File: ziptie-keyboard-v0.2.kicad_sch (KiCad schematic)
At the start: 147 parts, among them SW1 RotaryEncoder, U1 nice_nano

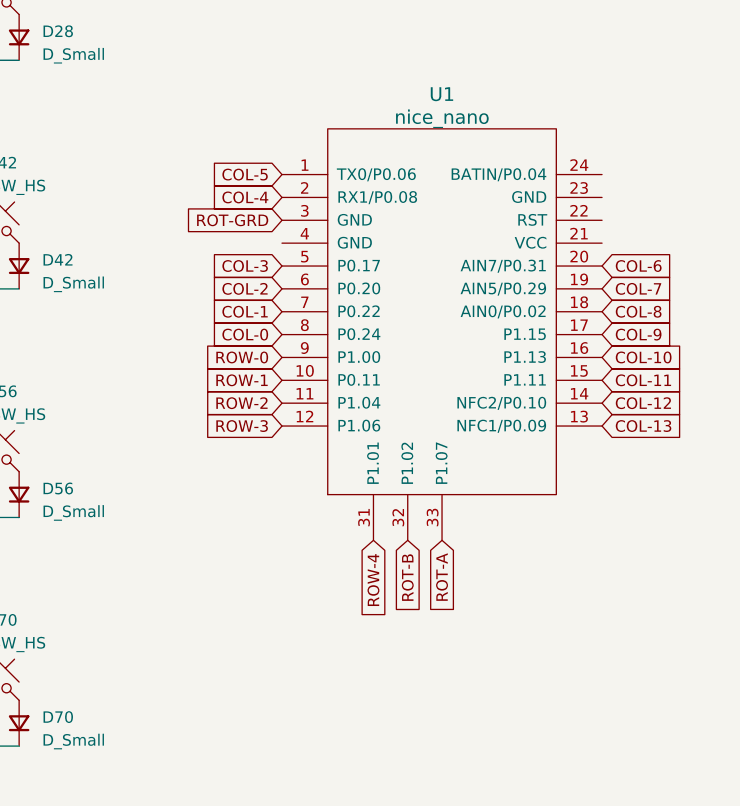
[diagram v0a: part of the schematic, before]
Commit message: Updated traces to 1mm and traced matrix
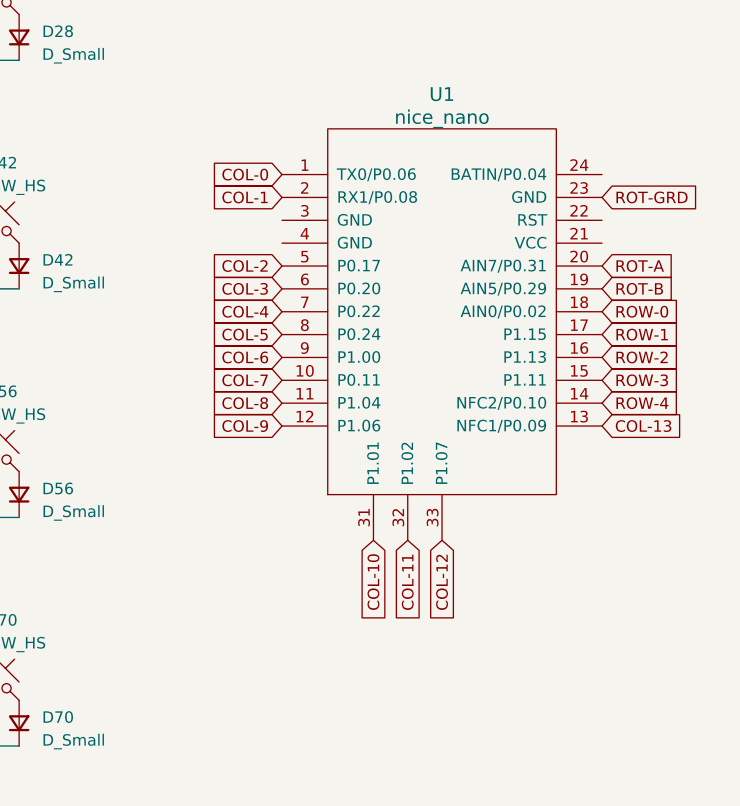
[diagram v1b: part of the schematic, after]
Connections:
- net COL-0: now also U1.1 (TX0/P0.06); no longer U1.8 (P0.24)
- net COL-1: now also U1.2 (RX1/P0.08); no longer U1.7 (P0.22)
- net COL-10: now also U1.31 (P1.01); no longer U1.16 (P1.13)
- net COL-11: now also U1.32 (P1.02); no longer U1.15 (P1.11)
- net COL-12: now also U1.33 (P1.07); no longer U1.14 (NFC2/P0.10)
- net COL-2: now also U1.5 (P0.17); no longer U1.6 (P0.20)
- net COL-3: now also U1.6 (P0.20); no longer U1.5 (P0.17)
- net COL-4: now also U1.7 (P0.22); no longer U1.2 (RX1/P0.08)
- net COL-5: now also U1.8 (P0.24); no longer U1.1 (TX0/P0.06)
- net COL-6: now also U1.9 (P1.00); no longer U1.20 (AIN7/P0.31)
- net COL-7: now also U1.10 (P0.11); no longer U1.19 (AIN5/P0.29)
- net COL-8: now also U1.11 (P1.04); no longer U1.18 (AIN0/P0.02)
- net COL-9: now also U1.12 (P1.06); no longer U1.17 (P1.15)
- net ROT-A: now also U1.20 (AIN7/P0.31); no longer U1.33 (P1.07)
- net ROT-B: now also U1.19 (AIN5/P0.29); no longer U1.32 (P1.02)
- net ROT-GRD: now also U1.23 (GND); no longer U1.3 (GND)
- net ROW-0: now also U1.18 (AIN0/P0.02); no longer U1.9 (P1.00)
- net ROW-1: now also U1.17 (P1.15); no longer U1.10 (P0.11)
- net ROW-2: now also U1.16 (P1.13); no longer U1.11 (P1.04)
- net ROW-3: now also U1.15 (P1.11); no longer U1.12 (P1.06)
- net ROW-4: now also U1.14 (NFC2/P0.10); no longer U1.31 (P1.01)

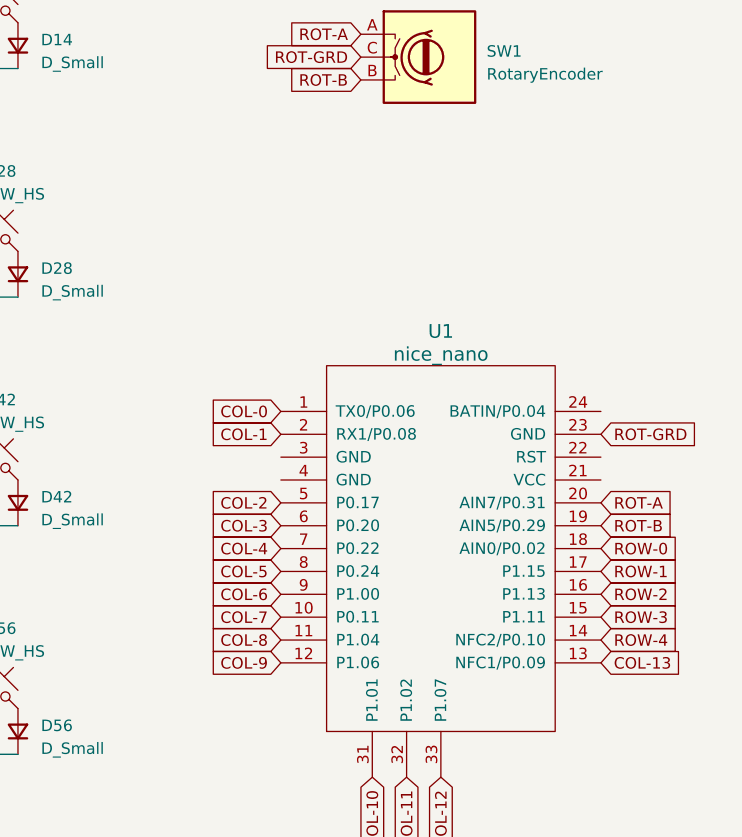
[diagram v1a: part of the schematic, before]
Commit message: Added traces and board cuts
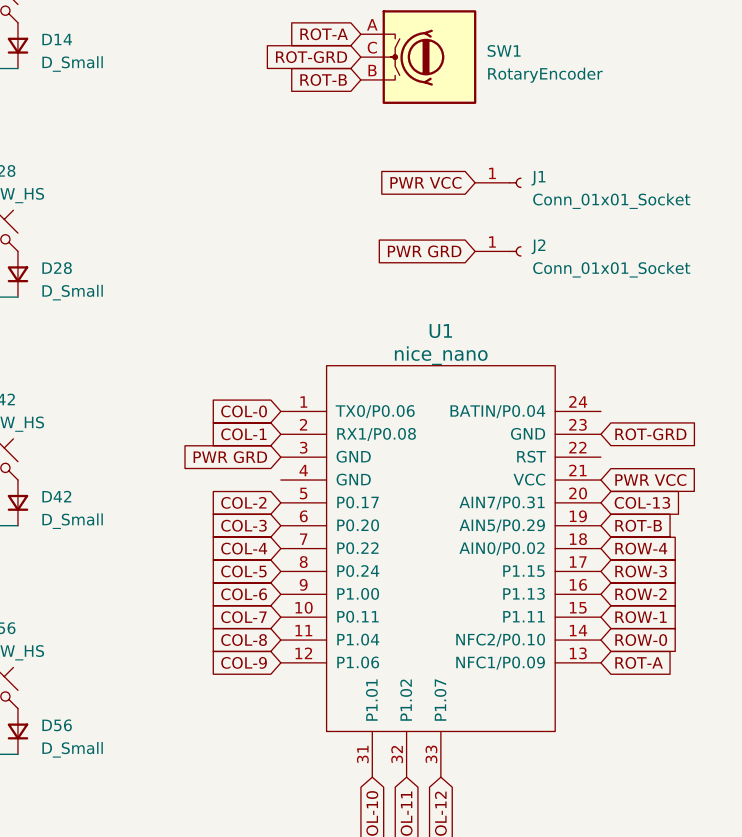
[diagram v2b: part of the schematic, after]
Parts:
- added J1, J2: Conn_01x01_Socket, Connector_Wire:SolderWire-0.1sqmm_1x01_D0.4mm_OD1mm, symbol Connector:Conn_01x01_Socket
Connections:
- net COL-13: now also U1.20 (AIN7/P0.31); no longer U1.13 (NFC1/P0.09)
- net ROT-A: now also U1.13 (NFC1/P0.09); no longer U1.20 (AIN7/P0.31)
- net ROW-0: now also U1.14 (NFC2/P0.10); no longer U1.18 (AIN0/P0.02)
- net ROW-1: now also U1.15 (P1.11); no longer U1.17 (P1.15)
- net ROW-3: now also U1.17 (P1.15); no longer U1.15 (P1.11)
- net ROW-4: now also U1.18 (AIN0/P0.02); no longer U1.14 (NFC2/P0.10)
- net PWR VCC: now reaches U1.21 (VCC)
- net PWR VCC: now also J1.1 (Pin_1)
- net PWR GRD: now reaches U1.3 (GND)
- net PWR GRD: now also J2.1 (Pin_1)
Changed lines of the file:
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@@
+    )
+  )
+  (global_label "PWR GRD" (shape input) (at 229.87 91.44 180) (fields_autoplaced)
+    (effects (font (size 1.27 1.27)) (justify right))
+    (property "Intersheetrefs" "${INTERSHEET_REFS}" (at 218.1952 91.44 0)
+      (effects (font (size 1.27 1.27)) (justify right) hide)
     )
   )
@@
     )
   )
-  (global_label "ROT-A" (shape input) (at 265.43 96.52 0) (fields_autoplaced)
+  (global_label "PWR VCC" (shape input) (at 265.43 93.98 0) (fields_autoplaced)
     (effects (font (size 1.27 1.27)) (justify left))
-    (property "Intersheetrefs" "${INTERSHEET_REFS}" (at 274.5649 96.52 0)
+    (property "Intersheetrefs" "${INTERSHEET_REFS}" (at 276.9234 93.98 0)
+      (effects (font (size 1.27 1.27)) (justify left) hide)
+    )
+  )
+  (global_label "ROT-A" (shape input) (at 265.43 114.3 0) (fields_autoplaced)
+    (effects (font (size 1.27 1.27)) (justify left))
+    (property "Intersheetrefs" "${INTERSHEET_REFS}" (at 274.5649 114.3 0)
       (effects (font (size 1.27 1.27)) (justify left) hide)
     )
@@
     )
   )
-  (global_label "ROW-3" (shape input) (at 265.43 109.22 0) (fields_autoplaced)
+  (global_label "ROW-3" (shape input) (at 265.43 104.14 0) (fields_autoplaced)
     (effects (font (size 1.27 1.27)) (justify left))
-    (property "Intersheetrefs" "${INTERSHEET_REFS}" (at 275.1696 109.22 0)
+    (property "Intersheetrefs" "${INTERSHEET_REFS}" (at 275.1696 104.14 0)
       (effects (font (size 1.27 1.27)) (justify left) hide)
     )
@@
     )
   )
-  (global_label "COL-13" (shape input) (at 265.43 114.3 0) (fields_autoplaced)
+  (global_label "PWR VCC" (shape input) (at 251.46 60.96 180) (fields_autoplaced)
+    (effects (font (size 1.27 1.27)) (justify right))
+    (property "Intersheetrefs" "${INTERSHEET_REFS}" (at 239.9666 60.96 0)
+      (effects (font (size 1.27 1.27)) (justify right) hide)
+    )
+  )
+  (global_label "COL-13" (shape input) (at 265.43 96.52 0) (fields_autoplaced)
     (effects (font (size 1.27 1.27)) (justify left))
-    (property "Intersheetrefs" "${INTERSHEET_REFS}" (at 275.9558 114.3 0)
+    (property "Intersheetrefs" "${INTERSHEET_REFS}" (at 275.9558 96.52 0)
       (effects (font (size 1.27 1.27)) (justify left) hide)
     )
   )
-  (global_label "ROW-1" (shape input) (at 265.43 104.14 0) (fields_autoplaced)
+  (global_label "ROW-1" (shape input) (at 265.43 109.22 0) (fields_autoplaced)
     (effects (font (size 1.27 1.27)) (justify left))
-    (property "Intersheetrefs" "${INTERSHEET_REFS}" (at 275.1696 104.14 0)
+    (property "Intersheetrefs" "${INTERSHEET_REFS}" (at 275.1696 109.22 0)
       (effects (font (size 1.27 1.27)) (justify left) hide)
     )
@@
     )
   )
-  (global_label "ROW-0" (shape input) (at 265.43 101.6 0) (fields_autoplaced)
+  (global_label "ROW-0" (shape input) (at 265.43 111.76 0) (fields_autoplaced)
     (effects (font (size 1.27 1.27)) (justify left))
-    (property "Intersheetrefs" "${INTERSHEET_REFS}" (at 275.1696 101.6 0)
+    (property "Intersheetrefs" "${INTERSHEET_REFS}" (at 275.1696 111.76 0)
       (effects (font (size 1.27 1.27)) (justify left) hide)
     )
@@
     )
   )
-  (global_label "ROW-4" (shape input) (at 265.43 111.76 0) (fields_autoplaced)
+  (global_label "ROW-4" (shape input) (at 265.43 101.6 0) (fields_autoplaced)
     (effects (font (size 1.27 1.27)) (justify left))
-    (property "Intersheetrefs" "${INTERSHEET_REFS}" (at 275.1696 111.76 0)
+    (property "Intersheetrefs" "${INTERSHEET_REFS}" (at 275.1696 101.6 0)
       (effects (font (size 1.27 1.27)) (justify left) hide)
     )
@@
     (property "Intersheetrefs" "${INTERSHEET_REFS}" (at 132.08 21.1637 90)
       (effects (font (size 1.27 1.27)) (justify left) hide)
+    )
+  )
+  (global_label "PWR GRD" (shape input) (at 251.46 68.58 180) (fields_autoplaced)
+    (effects (font (size 1.27 1.27)) (justify right))
+    (property "Intersheetrefs" "${INTERSHEET_REFS}" (at 239.7852 68.58 0)
+      (effects (font (size 1.27 1.27)) (justify right) hide)
     )
   )
@@
     )
   )
+  (symbol (lib_id "Connector:Conn_01x01_Socket") (at 256.54 60.96 0) (unit 1)
+    (in_bom yes) (on_board yes) (dnp no) (fields_autoplaced)
+    (property "Reference" "J1" (at 257.81 60.325 0)
+      (effects (font (size 1.27 1.27)) (justify left))
+    )
+    (property "Value" "Conn_01x01_Socket" (at 257.81 62.865 0)
+      (effects (font (size 1.27 1.27)) (justify left))
+    )
+    (property "Footprint" "Connector_Wire:SolderWire-0.1sqmm_1x01_D0.4mm_OD1mm" (at 256.54 60.96 0)
+      (effects (font (size 1.27 1.27)) hide)
+    )
+    (property "Datasheet" "~" (at 256.54 60.96 0)
+      (effects (font (size 1.27 1.27)) hide)
+    )
+    (pin "1")
+    (instances
+      (project "ziptie-keyboard-v0.2"
+        (path "/32677d6d-f5c2-46e9-b63f-fb92156b1d8b"
+          (reference "J1") (unit 1)
+        )
+      )
+    )
+  )
   (symbol (lib_id "marbastlib-choc:choc_SW_HS") (at 121.92 142.24 0) (unit 1)
     (in_bom yes) (on_board yes) (dnp no) (fields_autoplaced)
@@
         )
       )
+    )
+  )
+  (symbol (lib_id "Connector:Conn_01x01_Socket") (at 256.54 68.58 0) (unit 1)
+    (in_bom yes) (on_board yes) (dnp no) (fields_autoplaced)
+    (property "Reference" "J2" (at 257.81 67.945 0)
+      (effects (font (size 1.27 1.27)) (justify left))
+    )
+    (property "Value" "Conn_01x01_Socket" (at 257.81 70.485 0)
+      (effects (font (size 1.27 1.27)) (justify left))
+    )
+    (property "Footprint" "Connector_Wire:SolderWire-0.1sqmm_1x01_D0.4mm_OD1mm" (at 256.54 68.58 0)
+      (effects (font (size 1.27 1.27)) hide)
+    )
+    (property "Datasheet" "~" (at 256.54 68.58 0)
+      (effects (font (size 1.27 1.27)) hide)
+    )
+    (pin "1")
+    (instances
+      (project "ziptie-keyboard-v0.2"
+        (path "/32677d6d-f5c2-46e9-b63f-fb92156b1d8b"
+          (reference "J2") (unit 1)
+        )
+      )
